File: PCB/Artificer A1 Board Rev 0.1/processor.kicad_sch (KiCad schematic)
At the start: 8 parts, among them U1 T527M00X0DCH

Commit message: cleaned up, kicad 10 & usb c pd
migrated to Kicad 10,
added USB PD for power input
added capacitors inductors and resistor footprints
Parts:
- removed R54: 1k, symbol Device:R
- removed R58, R62, R74: 1k, symbol Device:R_Small
- removed R59, R60, R61: 200, symbol Device:R_Small
- added C85, C86, C87, C88: 100nF, PCM_JLCPCB:C_0402, symbol PCM_JLCPCB-Capacitors:0402,100nF,(2)
- added R32, R33, R37, R38: 1kΩ, PCM_JLCPCB:R_0402, symbol PCM_JLCPCB-Resistors:0402,1kΩ
- added R34, R35, R36: 200Ω, PCM_JLCPCB:R_0402, symbol PCM_JLCPCB-Resistors:0402,200Ω
- renumbered U1 to U8
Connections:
- net GND: now also R33.1, R34.2, R35.2, R36.2, R37.2, R38.1
- net HS-MIC: now also R32.1
- net PCIE-REF-CLKN: now also C85.1; no longer U8.C21 (PCIEREFCLKN)
- net PCIE-REF-CLKP: now also C86.1; no longer U8.B21 (PCIEREFCLKP)
- net PCIE-RX0-DN: no longer U8.C23 (PCIERX0-DN/US)
- net PCIE-RX0-DP: no longer U8.B23 (PCIERX0-DP/US)
- net PCIE-TX0-DN: now also C87.1; no longer U8.B22 (PCIETX0-DN/USB)
- net PCIE-TX0-DP: now also C88.1; no longer U8.A22 (PCIETX0-DP/USB)
- net at U8.G20 (USB2-REXT): now also R36.1
- net at U8.AJ1 (MICDET): now also R32.2
- net at U8.E20 (PCIEREXT): now also R38.2
- net USB2-DP: now reaches U8.D22 (USB2-DP)
- net USB2-DM: now reaches U8.E22 (USB2-DM)
- net at U8.F26 (HREXT): now also R33.2
- net at U8.F28 (EDPREXT): now also R37.1
- net at U8.G22 (USB0-REXT): now also R34.1
- net at U8.G24 (USB1-REXT): now also R35.1
- net RGMII0-CLKIN renamed ETH0.RGMII-CLKIN
- net RGMII0-MDC renamed ETH0.RGMII-MDC
- net RGMII0-MDIO renamed ETH0.RGMII-MDIO
- net RGMII0-RXCK renamed ETH0.RGMII-RXCK
- net RGMII0-RXCTL renamed ETH0.RGMII-RXCTL
- net RGMII0-RXD0 renamed ETH0.RGMII-RXD0
- net RGMII0-RXD1 renamed ETH0.RGMII-RXD1
- net RGMII0-RXD2 renamed ETH0.RGMII-RXD2
- net RGMII0-RXD3 renamed ETH0.RGMII-RXD3
- net RGMII0-TXCK renamed ETH0.RGMII-TXCK
- net RGMII0-TXCTL renamed ETH0.RGMII-TXCTL
- net RGMII0-TXD0 renamed ETH0.RGMII-TXD0
- net RGMII0-TXD1 renamed ETH0.RGMII-TXD1
- net RGMII0-TXD2 renamed ETH0.RGMII-TXD2
- net RGMII0-TXD3 renamed ETH0.RGMII-TXD3
- net RGMII1-CLKIN renamed ETH1.RGMII-CLKIN
- net RGMII1-MDC renamed ETH1.RGMII-MDC
- net RGMII1-MDIO renamed ETH1.RGMII-MDIO
- net RGMII1-RXCK renamed ETH1.RGMII-RXCK
- net RGMII1-RXCTL renamed ETH1.RGMII-RXCTL
- net RGMII1-RXD0 renamed ETH1.RGMII-RXD0
- net ETH1.RGMII-RXD0: no longer U8.F2 (PJ5)
- net RGMII1-RXD1 renamed ETH1.RGMII-RXD1
- net RGMII1-RXD2 renamed ETH1.RGMII-RXD2
- net RGMII1-RXD3 renamed ETH1.RGMII-RXD3
- net RGMII1-TXCK renamed ETH1.RGMII-TXCK
- net RGMII1-TXCTL renamed ETH1.RGMII-TXCTL
- net RGMII1-TXD1 renamed ETH1.RGMII-TXD1
- net RGMII1-TXD2 renamed ETH1.RGMII-TXD2
- net RGMII1-TXD3 renamed ETH1.RGMII-TXD3
- new net: C88.2, U8.A22 (PCIETX0-DP/USB)
- new net: C86.2, U8.B21 (PCIEREFCLKP)
- new net: C87.2, U8.B22 (PCIETX0-DN/USB)
- new net: C85.2, U8.C21 (PCIEREFCLKN)
- new net ETH1.RGMII-TXD0: U8.F2 (PJ5)
- no-connect marks 10 -> 8
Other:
- note added: "1.8V"
- note added: "3.3V"
- note added: "Close to SoC AO"
- note added: "No need for caps on the recieving line as the periferal card should have them."
- note added: "These pins are used for headphones and negative charge pumps."
- moved on the sheet: U8C, U8D

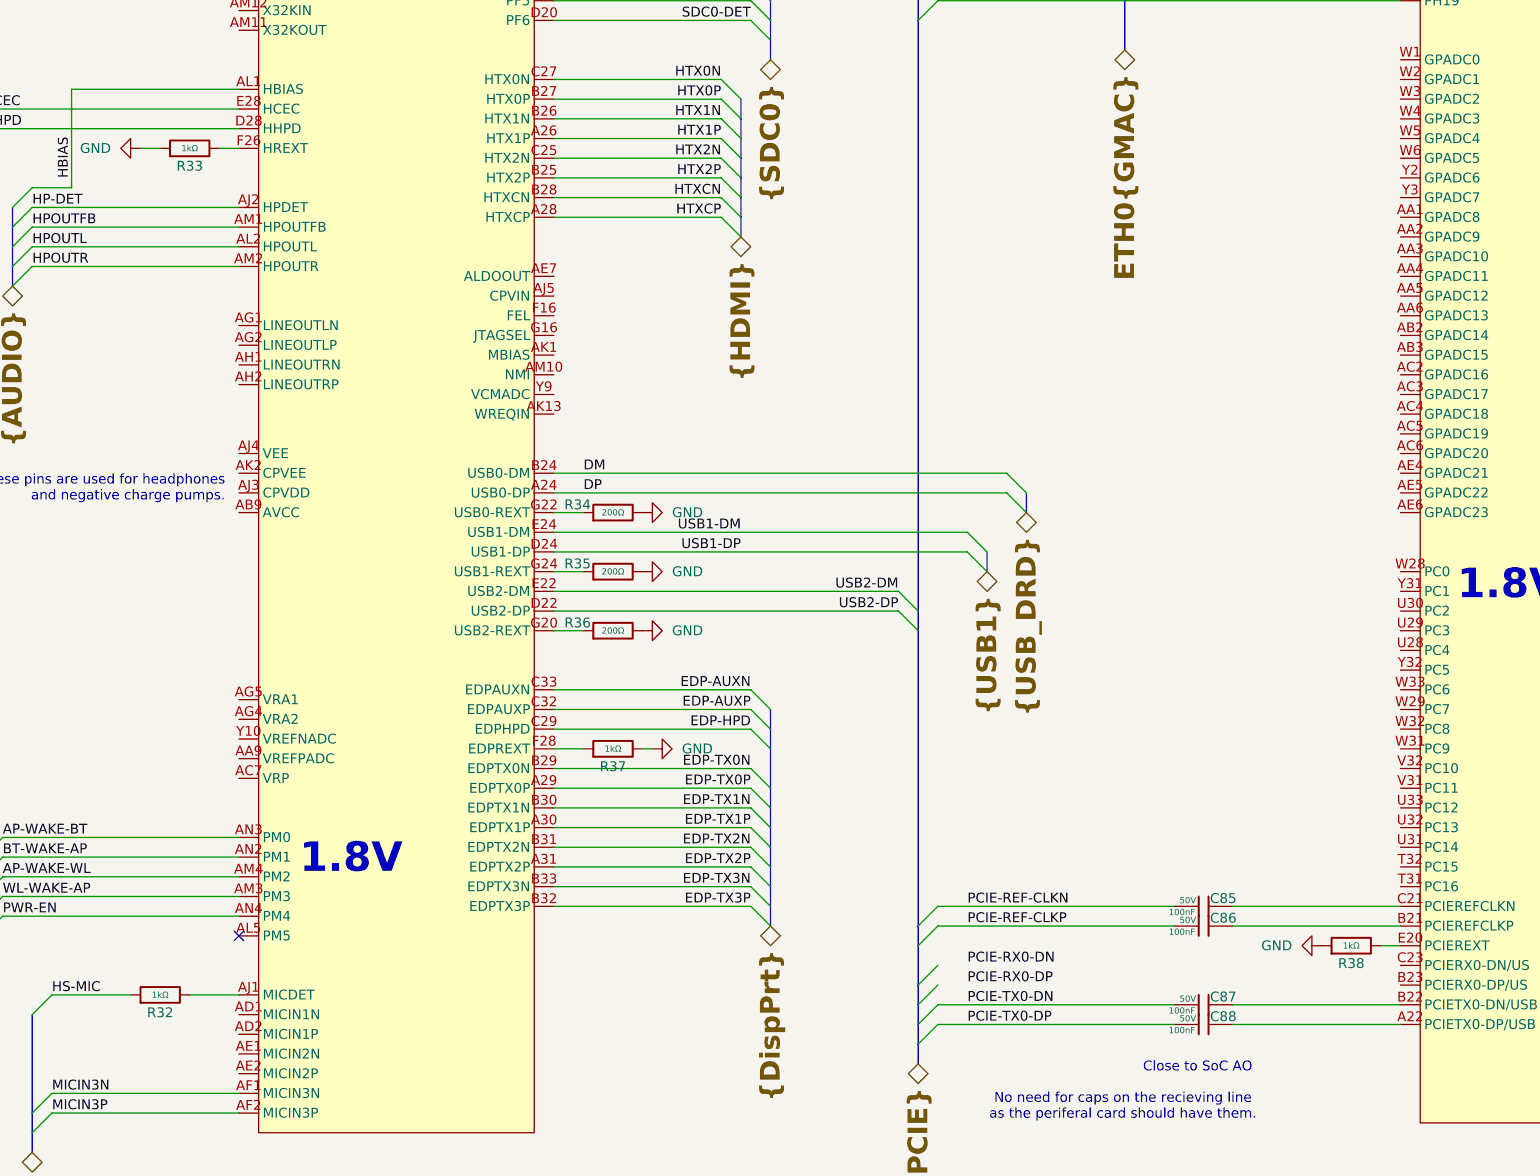
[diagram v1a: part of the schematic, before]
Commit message: placed all components
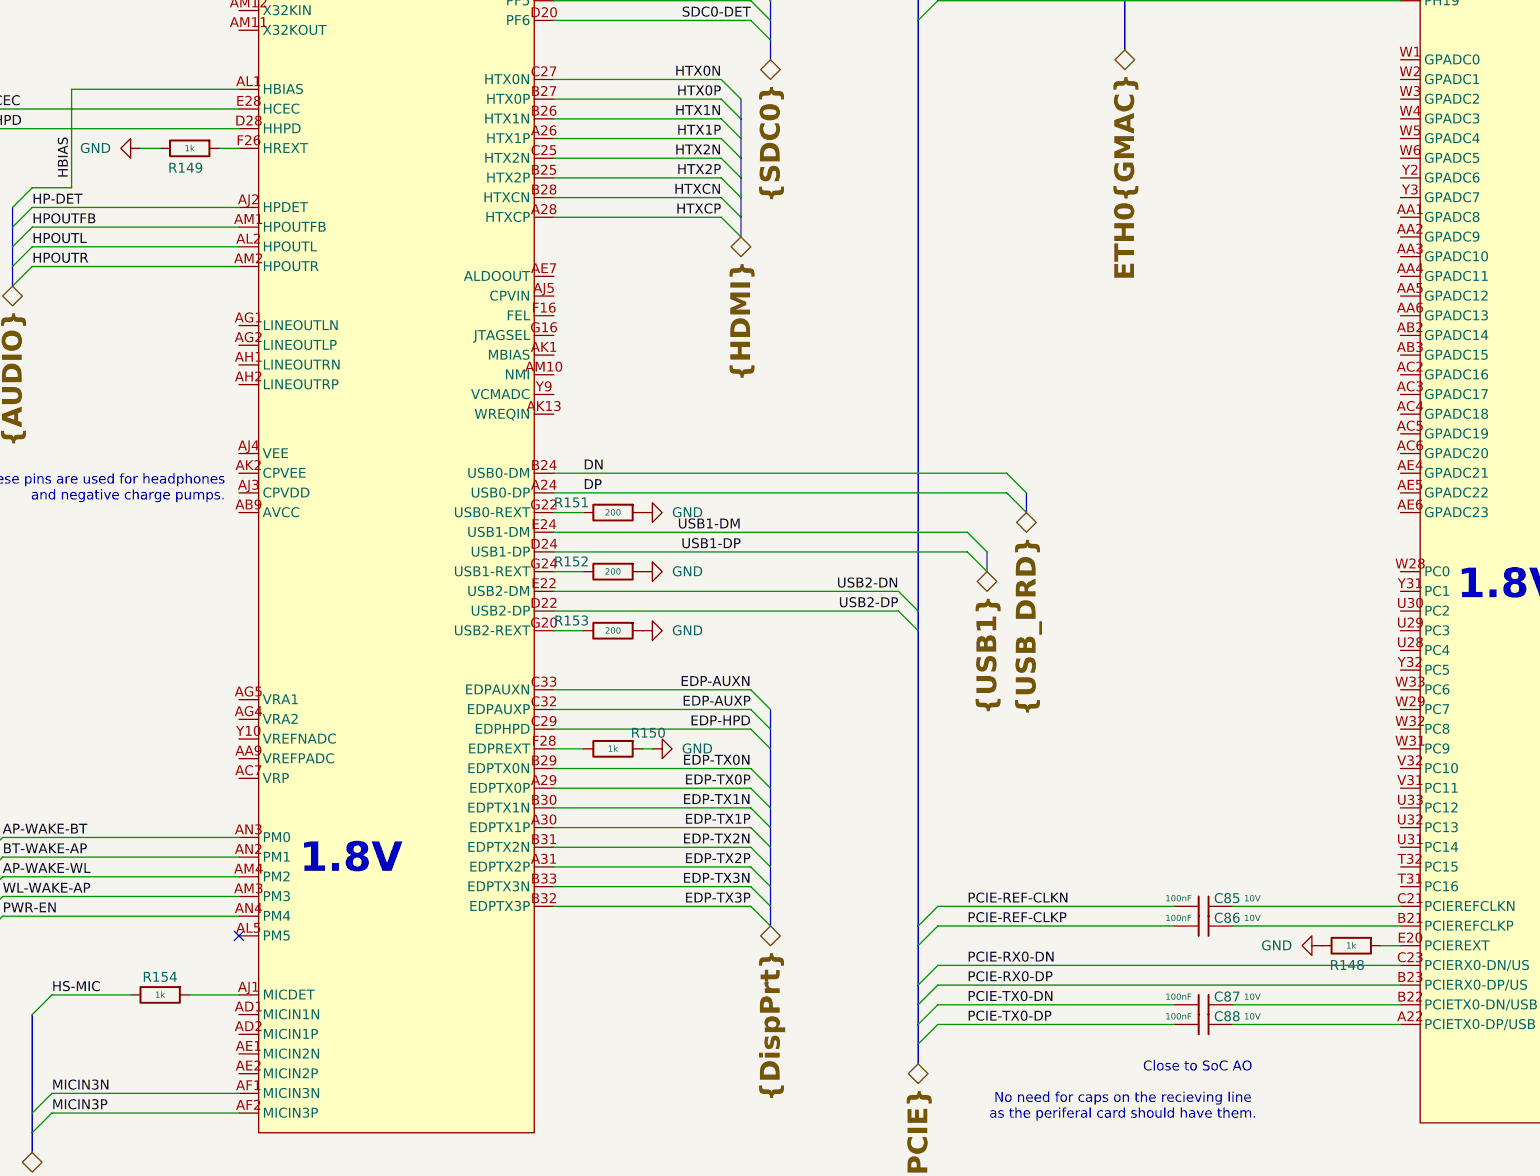
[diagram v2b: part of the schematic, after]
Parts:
- removed C85, C86, C87, C88: 100nF, PCM_JLCPCB:C_0402, symbol PCM_JLCPCB-Capacitors:0402,100nF,(2)
- removed R32, R33, R37, R38: 1kΩ, PCM_JLCPCB:R_0402, symbol PCM_JLCPCB-Resistors:0402,1kΩ
- removed R34, R35, R36: 200Ω, PCM_JLCPCB:R_0402, symbol PCM_JLCPCB-Resistors:0402,200Ω
- added C85, C86, C87, C88: 100nF, Capacitor_SMD:C_0201_0603Metric, symbol Cap:JLCPCB_Lib_Blank_Cap
- added R148, R149, R150, R154: 1k, Resistor_SMD:R_0201_0603Metric, symbol Cap:JLCPCB_Res_Custom
- added R151, R152, R153: 200, Resistor_SMD:R_0201_0603Metric, symbol Cap:JLCPCB_Res_Custom
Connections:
- net GND: now also R148.2, R149.2, R150.1, R151.1, R152.1, R153.1
- net HS-MIC: now also R154.2
- net PCIE-REF-CLKN: now also C85.1
- net PCIE-REF-CLKP: now also C86.1
- net PCIE-RX0-DN: now also U8.C23 (PCIERX0-DN/US)
- net PCIE-RX0-DP: now also U8.B23 (PCIERX0-DP/US)
- net PCIE-TX0-DN: now also C87.1
- net PCIE-TX0-DP: now also C88.1
- net at U8.A22 (PCIETX0-DP/USB): now also C88.2
- net at U8.B21 (PCIEREFCLKP): now also C86.2
- net at U8.B22 (PCIETX0-DN/USB): now also C87.2
- net at U8.C21 (PCIEREFCLKN): now also C85.2
- net at U8.E20 (PCIEREXT): now also R148.1
- net at U8.AJ1 (MICDET): now also R154.1
- net at U8.F26 (HREXT): now also R149.1
- net at U8.F28 (EDPREXT): now also R150.2
- net at U8.G20 (USB2-REXT): now also R153.2
- net at U8.G22 (USB0-REXT): now also R151.2
- net at U8.G24 (USB1-REXT): now also R152.2
- net DM renamed DN
- net USB2-DM renamed USB2-DN

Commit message: started routing
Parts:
- added C173: 100nF, Capacitor_SMD:C_0201_0603Metric, symbol Cap:JLCPCB_Lib_Blank_Cap
- added R204, R205: 10k, Resistor_SMD:R_0201_0603Metric, symbol Cap:JLCPCB_Res_Custom
- added U2: GD25LQ128EWIGR, easyeda:WSON-8_L6.0-W5.0-P1.27-BL-EP, symbol easyeda:GD25LQ128EWIGR
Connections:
- net GND: now also C173.1, U2.4 (VSS), U2.9 (EP)
- net SPI0_DI: now reaches U8.U28 (PC4)
- net SPI0_DI: now also U2.2 (SO(IO1))
- net SPI0_CS: now reaches U8.U29 (PC3)
- net SPI0_CS: now also U2.1 (~{CS})
- net SPI0_DO: now reaches U8.U30 (PC2)
- net SPI0_DO: now also U2.5 (SI(IO0))
- net SPI0_CLK: now reaches U8.V31 (PC11)
- net SPI0_CLK: now also U2.6 (SCLK)
- net USB1-DM renamed USB1-DN
- new net SPI0_HOLD: R204.2, U2.7 (HOLD#(IO3))
- new net SPI0_WP: R205.2, U2.3 (WP#(IO2))
- new net VCCIO_FLASH: C173.2, R204.1, R205.1, U2.8 (VCC)

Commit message: finsihed more routing
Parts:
- added C304, C305, C306, C307: 12pF, Capacitor_SMD:C_0201_0603Metric, symbol Cap:JLCPCB_Lib_Blank_Cap
- added R206: 10M, Resistor_SMD:R_0201_0603Metric, symbol Cap:JLCPCB_Res_Custom
- added R207: 4.3k, Resistor_SMD:R_0201_0603Metric, symbol Cap:JLCPCB_Res_Custom
- added R208: 6.8k, Resistor_SMD:R_0201_0603Metric, symbol Cap:JLCPCB_Res_Custom
- added R209, R210, R211, R212, R213, R214: 10k, Resistor_SMD:R_0201_0603Metric, symbol Cap:JLCPCB_Res_Custom
- added X4: 25MHz, Crystal:Crystal_SMD_3225-4Pin_3.2x2.5mm, symbol Device:Crystal_GND24
- added X5: SC-20S32.768kHz20PPM9pF, easyeda:OSC-SMD_L2.0-W1.2, symbol easyeda:SC-20S32.768kHz20PPM9pF
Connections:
- net GND: now also C304.1, C305.1, C306.1, C307.1, R208.2, R209.2, R211.1, X4.2, X4.4
- net ETH0.RGMII-INTB: now reaches U8.B15 (PH13)
- net ETH0.RGMII-PHYRSTB: now reaches U8.D16 (PH8)
- net ETH1.RGMII-PHYRSTB: now reaches U8.G4 (PJ10)
- net ETH1.RGMII-INTB: now reaches U8.J1 (PJ16)
- net Disp0-SCL: now reaches U8.L31 (PD22)
- net Disp0-SDA: now reaches U8.L32 (PD23)
- net BOOT_SEL_ADC: now reaches U8.W1 (GPADC0)
- net BOOT_SEL_ADC: now also R207.2, R208.1
- net DDR-PARA-SEL-ADC1: now reaches U8.W2 (GPADC1)
- net DDR-PARA-SEL-ADC1: now also R209.1, R210.2
- net DDR-PARA-SEL-ADC2: now reaches U8.W3 (GPADC2)
- net DDR-PARA-SEL-ADC2: now also R211.2, R212.1
- net X32KOUT: now reaches U8.AM11 (X32KOUT)
- net X32KOUT: now also C307.2, R206.2, X5.2 (OSC2)
- net X32KIN: now reaches U8.AM12 (X32KIN)
- net X32KIN: now also C306.2, R206.1, X5.1 (OSC1)
- net DXIN: now reaches U8.AM13 (DXIN)
- net DXIN: now also C304.2, X4.1
- net DXOUT: now reaches U8.AN13 (DXOUT)
- net DXOUT: now also C305.2, X4.3
- net at U8.V2 (LRADC1): now also R214.1
- net at U8.V3 (LRADC0): now also R213.1
- net LED-EN-B: now reaches U8.A2 (PE7)
- net LED-EN-C: now reaches U8.A3 (PE6)
- net PMU-SDA: now reaches U8.AN5 (PL1)
- net PMU-SCK: now reaches U8.AN6 (PL0)
- net LED-EN-D: now reaches U8.B1 (PE9)
- net POWER-EN-D: now reaches U8.B2 (PE8)
- net POWER-EN-C: now reaches U8.B3 (PE5)
- net SCL-A: now reaches U8.C1 (PE12)
- net POWER-EN-A: now reaches U8.C2 (PE10)
- net SDA-C: now reaches U8.C3 (PE4)
- net SCL-B: now reaches U8.C4 (PE1)
- net SCL-C: now reaches U8.E4 (PE3)
- net SDA-B: now reaches U8.E5 (PE2)
- net POWER-EN-B: now reaches U8.E6 (PE0)
- net SDA-A: now reaches U8.G6 (PE13)
- net LED-EN-A: now reaches U8.J7 (PE11)
- net SCL-D: now reaches U8.L7 (PE14)
- net SDA-D: now reaches U8.N7 (PE15)
- net DBG_UART0_TX: now reaches U8.R28 (PB9)
- net DBG_UART0_RX: now reaches U8.R29 (PB10)
- net Disp1-SCL: now reaches U8.R30 (PB11)
- net Disp1-SDA: now reaches U8.R31 (PB12)
- net DN renamed DBG_DN
- net DP renamed DBG_DP
- net PCIE0-PERSTN  renamed PCIE0-PERSTN
- new net VCC-ADC: R207.1, R210.1, R212.2, R213.2, R214.2
- no-connect marks 8 -> 10
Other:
- note added: "TWI0"
- note added: "TWI1"
- note added: "TWI2"
- note added: "TWI3"
- note added: "TWI4"
- note added: "TWI5"
- note added: "remappable"
- moved on the sheet: C173, C85, C86, C87, C88, R148, R149, R150, R151, R152, R153, R154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

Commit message: more routing and decoupling
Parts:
- added C332, C333, C334, C335, C336, C337: 2.2uF, Capacitor_SMD:C_0201_0603Metric, symbol Cap:JLCPCB_Lib_Blank_Cap
- added C338, C339, C340: 470nF, Capacitor_SMD:C_0201_0603Metric, symbol Cap:JLCPCB_Lib_Blank_Cap
- added R227, R228: 4.7k, Resistor_SMD:R_0201_0603Metric, symbol Cap:JLCPCB_Res_Custom
- added R229, R232: 0Ω, Resistor_SMD:R_0201_0603Metric, symbol Cap:JLCPCB_Res_Custom
- added SW1: BOOT1, easyeda:SW-SMD_4P-L3.5-W3.0-P1.50-LS4.7, symbol easyeda:TS-1185-W-4P-H1.8-160
- added SW2: RESET, easyeda:SW-SMD_4P-L3.5-W3.0-P1.50-LS4.7, symbol easyeda:TS-1185-W-4P-H1.8-160
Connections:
- net AP-WAKE-BT: now also U8.AN2 (PM1); no longer U8.AN3 (PM0)
- net BT-WAKE-AP: now also U8.AN3 (PM0); no longer U8.AN2 (PM1)
- net GND: now also C332.1, C333.1, C334.1, C335.1, C336.1, R229.2, R232.2, SW1.3, SW2.3
- net PMU-SCK: now also R227.2
- net PMU-SDA: now also R228.2
- net PCIE-CARD-PRESENT: now reaches U8.L28 (PD20)
- net PCIE-SEL: now reaches U8.L29 (PD21)
- net AVCC: now reaches U8.AA9 (VREFPADC)
- net AVCC: now also U8.AB9 (AVCC), C337.2
- net VRP: now reaches U8.AC7 (VRP)
- net VRP: now also C340.2
- net ALDO-OUT: now reaches U8.AE7 (ALDOOUT)
- net ALDO-OUT: now also C332.2
- net VRA2: now reaches U8.AG4 (VRA2)
- net VRA2: now also C339.2
- net VRA1: now reaches U8.AG5 (VRA1)
- net VRA1: now also C338.2
- net AP-RESET: now reaches U8.AJ11 (RESET)
- net AP-RESET: now also SW2.1
- net CPVDD: now reaches U8.AJ3 (CPVDD)
- net CPVDD: now also C336.2
- net at U8.AJ4 (VEE): now also U8.AK2 (CPVEE), C335.2
- net CPVIN: now reaches U8.AJ5 (CPVIN)
- net CPVIN: now also C333.2
- net at U8.AK13 (WREQIN): now also R229.1
- net AP-NMI: now reaches U8.AM10 (NMI)
- net FEL: now reaches U8.F16 (FEL)
- net FEL: now also SW1.1
- net AGND: now reaches U8.Y10 (VREFNADC)
- net AGND: now also C337.1, C338.1, C339.1, C340.1, R232.1
- net VCM-ADC: now reaches U8.Y9 (VCMADC)
- net VCM-ADC: now also C334.2
- net PI1: now reaches U8.AG13 (PI1)
- net PI0: now reaches U8.AH13 (PI0)
- net PI7: now reaches U8.AH15 (PI7)
- net PI15: now reaches U8.AH17 (PI15)
- net PI5: now reaches U8.AJ15 (PI5)
- net PL13: now reaches U8.AJ7 (PL13)
- net PL11: now reaches U8.AJ9 (PL11)
- net PI6: now reaches U8.AK15 (PI6)
- net PI13: now reaches U8.AK17 (PI13)
- net PL12: now reaches U8.AK7 (PL12)
- net PL10: now reaches U8.AK9 (PL10)
- net PI2: now reaches U8.AL15 (PI2)
- net PI8: now reaches U8.AL16 (PI8)
- net PI12: now reaches U8.AL17 (PI12)
- net PL5: now reaches U8.AL7 (PL5)
- net PI4: now reaches U8.AM15 (PI4)
- net PI9: now reaches U8.AM16 (PI9)
- net PI11: now reaches U8.AM17 (PI11)
- net PI14: now reaches U8.AM18 (PI14)
- net PL3: now reaches U8.AM6 (PL3)
- net PL4: now reaches U8.AM7 (PL4)
- net PL7: now reaches U8.AM8 (PL7)
- net PL9: now reaches U8.AM9 (PL9)
- net PI3: now reaches U8.AN15 (PI3)
- net PI10: now reaches U8.AN17 (PI10)
- net PL2: now reaches U8.AN7 (PL2)
- net PL6: now reaches U8.AN8 (PL6)
- net PL8: now reaches U8.AN9 (PL8)
- new net VCC-3V3: R227.1, R228.1
- no-connect marks 10 -> 61
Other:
- note added: "Place right at BGA balls"
- note added: "S-PWM0-0"
- note added: "S-TWI0-SCK"
- note added: "S-TWI0-SDA"
- note added: "S-TWI1-SCK"
- note added: "S-TWI1-SDA"
- note added: "S-TWI2-SCK"
- note added: "S-TWI2-SDA"
- note added: "S-UART0-RX"
- note added: "S-UART0-TX"
- note added: "SPI1_CE0"
- note added: "SPI1_MISO"
- note added: "SPI1_MOSI"
- note added: "SPI1_SCLK"
- note added: "SPI2_CS0"
- note added: "SPI2_MISO"
- note added: "SPI2_MOSI"
- note added: "SPI2_SCLK"
- moved on the sheet: C173, C306, C307, R154, R204, R205, R206, U2, X5

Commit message: now the board is more manufacturable
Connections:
- net PCIE-DP: now reaches C88.2, U8.A22 (PCIETX0-DP/USB)
- net PCIE-CLKP: now reaches C86.2, U8.B21 (PCIEREFCLKP)
- net PCIE-DN: now reaches C87.2, U8.B22 (PCIETX0-DN/USB)
- net PCIE-CLKN: now reaches C85.2, U8.C21 (PCIEREFCLKN)
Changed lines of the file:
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@@
+		)
+	)
+	(label "PCIE-DP"
+		(at 302.26 217.17 0)
+		(effects
+			(font
+				(size 1.27 1.27)
+			)
+			(justify left bottom)
 		)
 	)
@@
 		)
 	)
+	(label "PCIE-DN"
+		(at 302.26 214.63 0)
+		(effects
+			(font
+				(size 1.27 1.27)
+			)
+			(justify left bottom)
+		)
+	)
 	(label "WL-WAKE-AP"
 		(at 147.32 200.66 0)
@@
 		)
 	)
+	(label "PCIE-CLKP"
+		(at 302.26 204.47 0)
+		(effects
+			(font
+				(size 1.27 1.27)
+			)
+			(justify left bottom)
+		)
+	)
 	(label "DSI1-CKN"
 		(at 391.16 64.77 180)
@@
 		(effects
 			(font
+				(size 1.27 1.27)
+			)
+			(justify left bottom)
+		)
+	)
+	(label "PCIE-CLKN"
+		(at 302.26 201.93 0)
+		(effects
+			(font

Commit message: finished most of the power
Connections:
- net Disp0-SCL: now also U8.R30 (PB11); no longer U8.L31 (PD22)
- net Disp0-SDA: now also U8.R31 (PB12); no longer U8.L32 (PD23)
- net Disp1-SCL: now also U8.L31 (PD22); no longer U8.R30 (PB11)
- net Disp1-SDA: now also U8.L32 (PD23); no longer U8.R31 (PB12)
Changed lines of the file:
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@@
 		)
 	)
-	(label "Disp1-SDA"
+	(label "Disp0-SDA"
 		(at 27.94 99.06 0)
 		(effects
@@
 		)
 	)
-	(label "Disp0-SCL"
+	(label "Disp1-SCL"
 		(at 370.84 82.55 180)
 		(effects
@@
 		)
 	)
-	(label "Disp0-SDA"
+	(label "Disp1-SDA"
 		(at 370.84 85.09 180)
 		(effects
@@
 		)
 	)
-	(label "Disp1-SCL"
+	(label "Disp0-SCL"
 		(at 27.94 96.52 0)
 		(effects
@@
 		)
 	)
-	(hierarchical_label "{DSI0}"
+	(hierarchical_label "{DSI1}"
 		(shape bidirectional)
 		(at 373.38 90.17 270)
@@
 		)
 	)
-	(hierarchical_label "{DSI1}"
+	(hierarchical_label "{DSI0}"
 		(shape bidirectional)
 		(at 25.4 104.14 270)

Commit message: optimized copper pour, added LEDs
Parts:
- added D17, D18: GREEN LED, LED_SMD:LED_0402_1005Metric, symbol Device:LED
- added R244, R245: 33k, Resistor_SMD:R_0201_0603Metric, symbol Cap:JLCPCB_Res_Custom
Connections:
- net GND: now also R244.1, R245.1
- net LED1: now reaches U8.N32 (PB5)
- net LED1: now also D17.2 (A)
- net LED2: now reaches U8.N33 (PB6)
- net LED2: now also D18.2 (A)
- new net: D17.1 (K), R244.2
- new net: D18.1 (K), R245.2
- no-connect marks 61 -> 59
